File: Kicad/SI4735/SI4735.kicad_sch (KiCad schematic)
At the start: 128 parts, among them IC1 SI4732-A10-GS, IC2 TCA9537DGSR, J1 Conn_01x03, J2 Conn_01x05, J3 Headphones, J5 DISP LEFT, J6 DISP RIGHT, J7 Conn_01x02_Pin, J8 TYPE-C-31-M-12, J9 Conn_01x02_Pin, Q2 2N7002, Q3 2SK508G-K51-AE3-R, SW1 SW_Push, T1 TestPoint, T10 TestPoint, T11 TestPoint, T5 TestPoint, T6 TestPoint, T7 TestPoint, T8 TestPoint, T9 TestPoint, U1 HT-CT62, U11 RT9013, U2 BME690, U4 LSM6DS3, U5 TPA6130A2RTJTR, U6 RT9013, U7 MAX98357AETE+T, U8 MAX98357AETE+T, U9 Si4735-D60-GU, X1 X322525MMB4SI, Y1 Si5351A-B-GT, Y2 RV-3032-C7

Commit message: Add files via upload
- Rotation of SI4732 Radio
- Added Battery Charging IC TP4057
- Added Light Sensor VEML7700
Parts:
- removed C33: 100nF, Capacitor_SMD:C_0603_1608Metric, symbol Device:C_Small
- added C10: 1uF, Capacitor_SMD:C_0603_1608Metric, symbol Device:C_Small
- added IC2: VEML7700, VEML7700:VEML7700, symbol VEML7700-TR:VEML7700-TR
- added JP1: Jumper_2_Small_Open, Jumper:SolderJumper-2_P1.3mm_Open_RoundedPad1.0x1.5mm, symbol Jumper:Jumper_2_Small_Open
- added R41: 2k, Resistor_SMD:R_0603_1608Metric, symbol Device:R_Small
- added U12: TP4057, Package_TO_SOT_SMD:TSOT-23-6, symbol Battery_Management:TP4057
- C1: renamed from C49; LCSC Part Name (none) -> C14663
- C11: renamed from C41; LCSC Part Name (none) -> C1656
- C12: renamed from C8; LCSC Part Name (none) -> C96446
- C13: renamed from C9; LCSC Part Name (none) -> C96446
- C14: renamed from C10; LCSC Part Name (none) -> C96446
- C15: renamed from C11; LCSC Part Name (none) -> C96446
- C16: renamed from C43; LCSC Part Name (none) -> C1656
- C17: renamed from C46; LCSC Part Name (none) -> C1656
- C18: renamed from C48; LCSC Part Name (none) -> C1623
- C19: renamed from C47; LCSC Part Name (none) -> C1656
- C2: renamed from C44; LCSC Part Name (none) -> C14663
- C20: renamed from C14; LCSC Part Name (none) -> C15849
- C21: renamed from C15; LCSC Part Name (none) -> C15849
- C22: renamed from C18; LCSC Part Name (none) -> C14663
- C23: renamed from C19; LCSC Part Name (none) -> C14663
- C24: renamed from C20; LCSC Part Name (none) -> C15849
- C25: renamed from C21; LCSC Part Name (none) -> C14663
- C26: renamed from C23; LCSC Part Name (none) -> C14663
- C27: LCSC Part Name (none) -> C14663
- C28: renamed from C24; LCSC Part Name (none) -> C14663
- C3: renamed from C16; LCSC Part Name (none) -> C15849
- C30: renamed from C34; value 270p -> 330pF; LCSC Part Name (none) -> C1664
- C31: renamed from C37; LCSC Part Name (none) -> C14663
- C32: renamed from C42; LCSC Part Name (none) -> C1653
- C33: renamed from C39; value 270p -> 330pF; LCSC Part Name (none) -> C1664
- C34: renamed from C28; LCSC Part Name (none) -> C28323
- C36: renamed from C29; LCSC Part Name (none) -> C28323
- C37: renamed from C30; LCSC Part Name (none) -> C28323
- C4: renamed from C22; LCSC Part Name (none) -> C14663
- C5: renamed from C38; LCSC Part Name (none) -> C1656
- C6: renamed from C17; LCSC Part Name (none) -> C14663
- C7: renamed from C32; LCSC Part Name (none) -> C21122
- C8: renamed from C36; LCSC Part Name (none) -> C1647
- C9: renamed from C40; LCSC Part Name (none) -> C1656
- D1: renamed from D7; LCSC Part Name (none) -> N.C.
- D2: renamed from D6; LCSC Part Name (none) -> N.C.
- IC1: LCSC Part Name C2155558 -> C2155558
- J1, L7, U+1, U-1: LCSC Part Name (none) -> N.C.
- J2: renamed from J9; LCSC Part Name (none) -> N.C.
- J3: renamed from J7; LCSC Part Name (none) -> N.C.
- J5: renamed from J3; LCSC Part Name (none) -> N.C.
- J6: renamed from J2; LCSC Part Name (none) -> N.C.
- J7: renamed from J5; LCSC Part Name (none) -> N.C.
- J8: renamed from J6; LCSC Part Name (none) -> N.C.
- L1: renamed from L4; LCSC Part Name (none) -> C18221279
- L2: renamed from L1; LCSC Part Name (none) -> C373725
- L3: renamed from L2; LCSC Part Name (none) -> C373725
- L4: renamed from L6; LCSC Part Name (none) -> C373725
- L5: footprint Inductor_SMD:L_0805_2012Metric_Pad1.15x1.40mm_HandSolder -> Inductor_SMD:L_0603_1608Metric_Pad1.05x0.95mm_HandSolder
- L6: renamed from L3; LCSC Part Name (none) -> C373725
- Q2: value 2N7002 -> SI2302
- R1: renamed from R45; LCSC Part Name (none) -> C15402
- R10: renamed from R41; LCSC Part Name (none) -> C22975
- R12: renamed from R48; LCSC Part Name (none) -> N.C.
- R13: renamed from R1; LCSC Part Name (none) -> C25804
- R14: renamed from R24; LCSC Part Name (none) -> C25804
- R17: renamed from R25; LCSC Part Name (none) -> C25804
- R18: renamed from R38; value 2k -> 0R; LCSC Part Name (none) -> C15402
- R19: renamed from R23; LCSC Part Name (none) -> C15402
- R2: renamed from R46; footprint Resistor_SMD:R_0805_2012Metric_Pad1.20x1.40mm_HandSolder -> Resistor_SMD:R_0603_1608Metric; LCSC Part Name (none) -> C15402
- R20: renamed from R15; LCSC C17414 -> C17477; LCSC Part Name (none) -> C17477
- R21: renamed from R27; LCSC Part Name (none) -> N.C.
- R22: renamed from R13; LCSC Part Name (none) -> C25804
- R23: renamed from R12; LCSC Part Name (none) -> C25804
- R24: renamed from R8; LCSC Part Name (none) -> C15402
- R25: renamed from R9; LCSC Part Name (none) -> C15402
- R26: renamed from R10; LCSC Part Name (none) -> N.C.
- R27: renamed from R11; LCSC Part Name (none) -> N.C.
- R28: LCSC Part Name (none) -> C15402
- R29: renamed from R39; LCSC Part Name (none) -> C15402
- R3: renamed from R40; LCSC Part Name (none) -> C22975
- R31: renamed from R26; LCSC Part Name (none) -> C15402
- R32: renamed from R18; LCSC Part Name (none) -> C25804
- R34: LCSC Part Name (none) -> C25804
- R36: renamed from R2; LCSC Part Name (none) -> C15402
- R37: renamed from R53; LCSC Part Name (none) -> C15402
- R38: renamed from R20; LCSC Part Name (none) -> C25804
- R39: renamed from R52; LCSC Part Name (none) -> C25804
- R4: renamed from R16; LCSC Part Name (none) -> C25803
- R40: renamed from R47; LCSC Part Name (none) -> C25804
- R5: renamed from R7; LCSC Part Name (none) -> C25803
- R6: renamed from R14; LCSC Part Name (none) -> N.C.
- R9: renamed from R42; LCSC Part Name (none) -> C23228
- T1: renamed from T6; LCSC Part Name (none) -> N.C.
- T2: renamed from T5; LCSC Part Name (none) -> N.C.
- T3: renamed from T11; LCSC Part Name (none) -> N.C.
- T4: renamed from T1; LCSC Part Name (none) -> N.C.
- T5: renamed from T7; LCSC Part Name (none) -> N.C.
- T6: renamed from T8; LCSC Part Name (none) -> N.C.
- T7: renamed from T9; LCSC Part Name (none) -> N.C.
- T8: renamed from T10; LCSC Part Name (none) -> N.C.
- U2: renamed from U8; LCSC Part Name (none) -> C910544
- U5: renamed from U2; LCSC Part Name (none) -> C42431867
- U6: renamed from U13; LCSC Part Name (none) -> C19270550
- Y2: LCSC Part Name (none) -> C5127802
- renumbered ANT0 to ANT2, ANT5 to ANT3, C45 to C35, D2 to D3, IC2 to IC3, J8 to J4, Q3 to Q1, R50 to R11, R49 to R15, R51 to R16, R22 to R30, R19 to R33, R44 to R35, R21 to R7, R17 to R8, U9 to U1, U4 to U10, U7 to U3, U5 to U4, U6 to U7, U1 to U8, U11 to U9
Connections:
- net +3.3VA: now also IC2.2 (VDD)
- net +5V: now also C10.1, JP1.2 (B), U12.3 (BAT); no longer J4.A4 (VBUS), J4.A9 (VBUS), J4.B4 (VBUS), J4.B9 (VBUS)
- net GND: now also C10.2, IC2.3 (GND), R41.1, U12.2 (GND)
- net SCL: now also IC2.1 (SCL)
- net SDA: now also IC2.4 (SDA)
- net at C30.1, R26.2: no longer J5.1 (Pin_1)
- new net: R41.2, U12.6 (PROG)
- new net +5VD: J4.A4 (VBUS), J4.A9 (VBUS), J4.B4 (VBUS), J4.B9 (VBUS), JP1.1 (A), U12.4 (V_{CC})
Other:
- note added: "Light Sensor"
- note added: "R18 Pad Umbaubar auf Quarz mit 22pF"
- moved on the sheet: J5

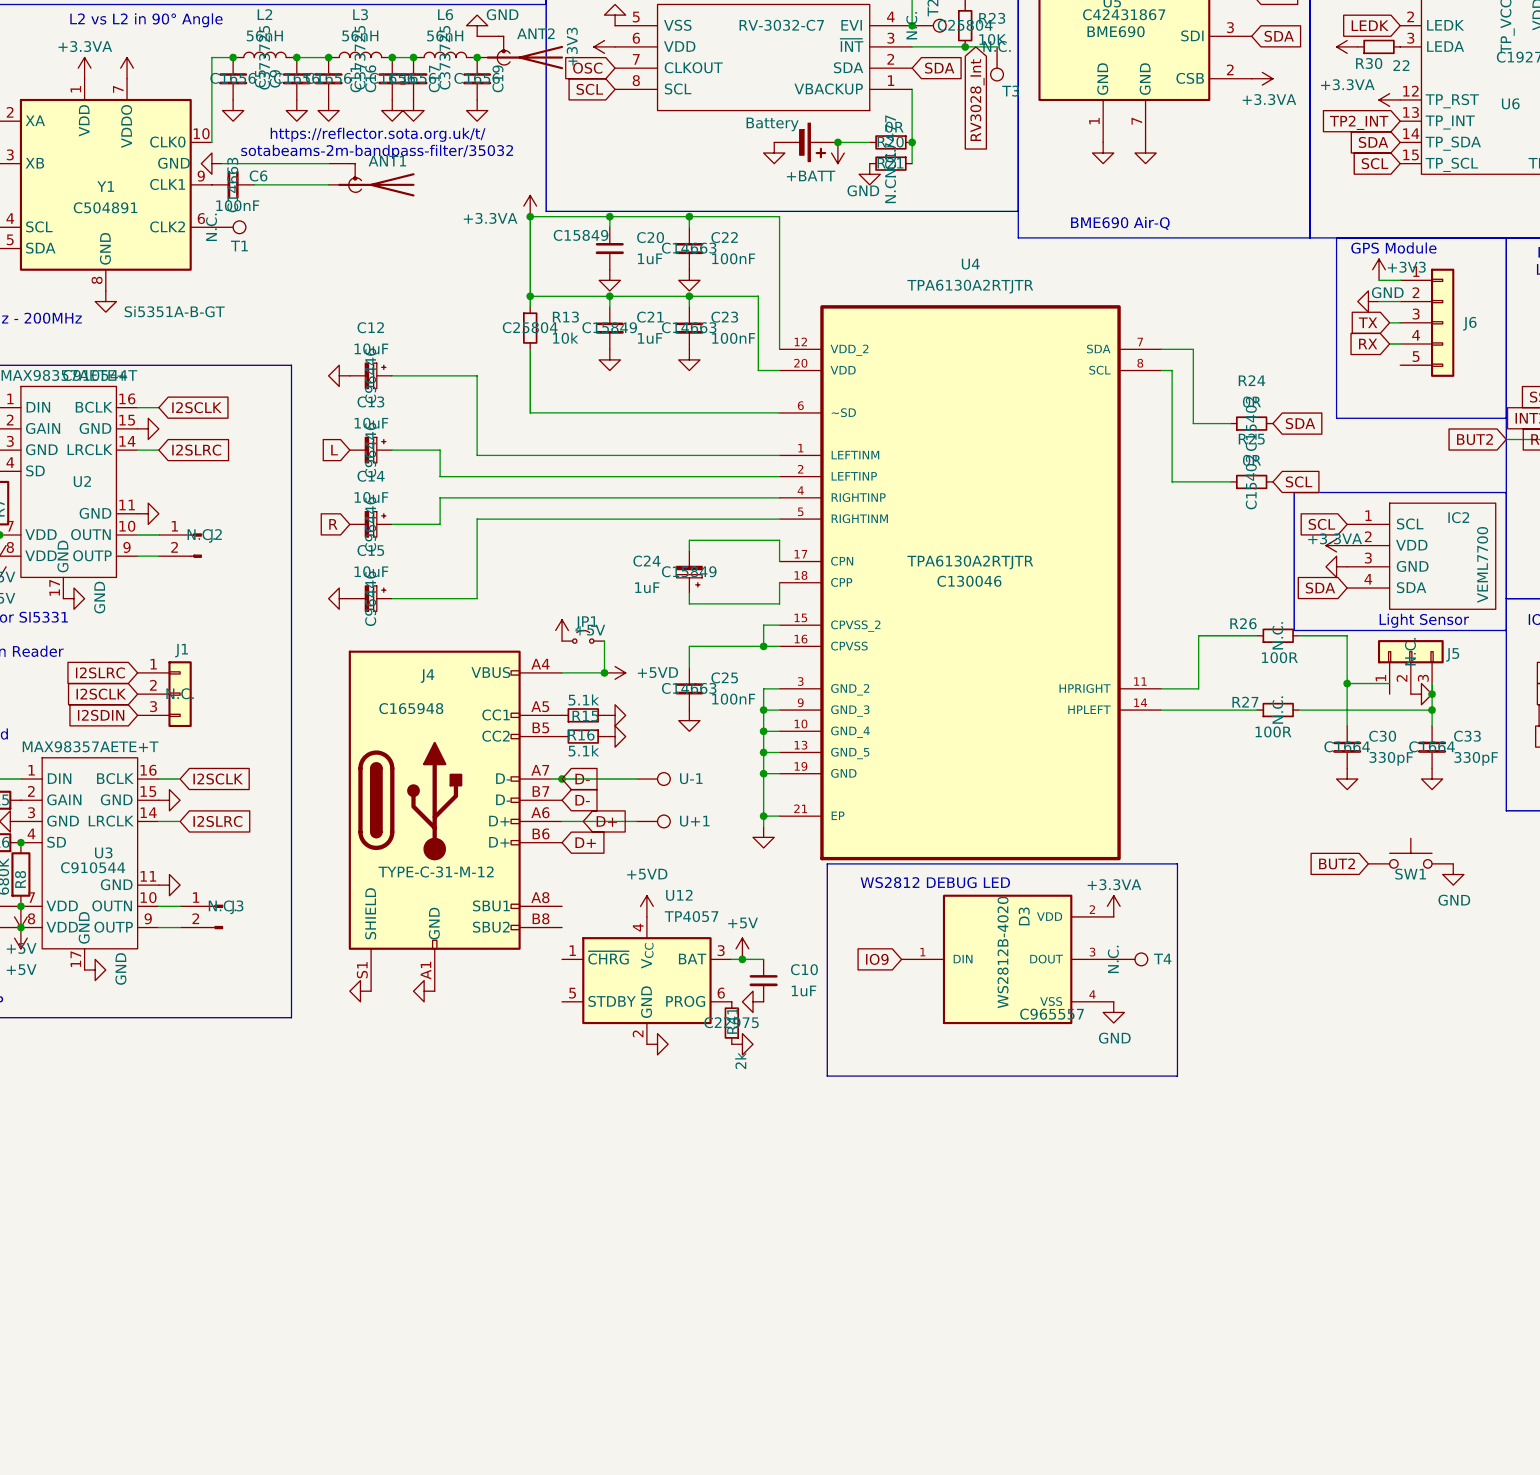
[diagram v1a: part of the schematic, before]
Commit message: Add files via upload
- Added MLX90640 Thermal Camera
- Refinement of inner Layers to enhance EMC
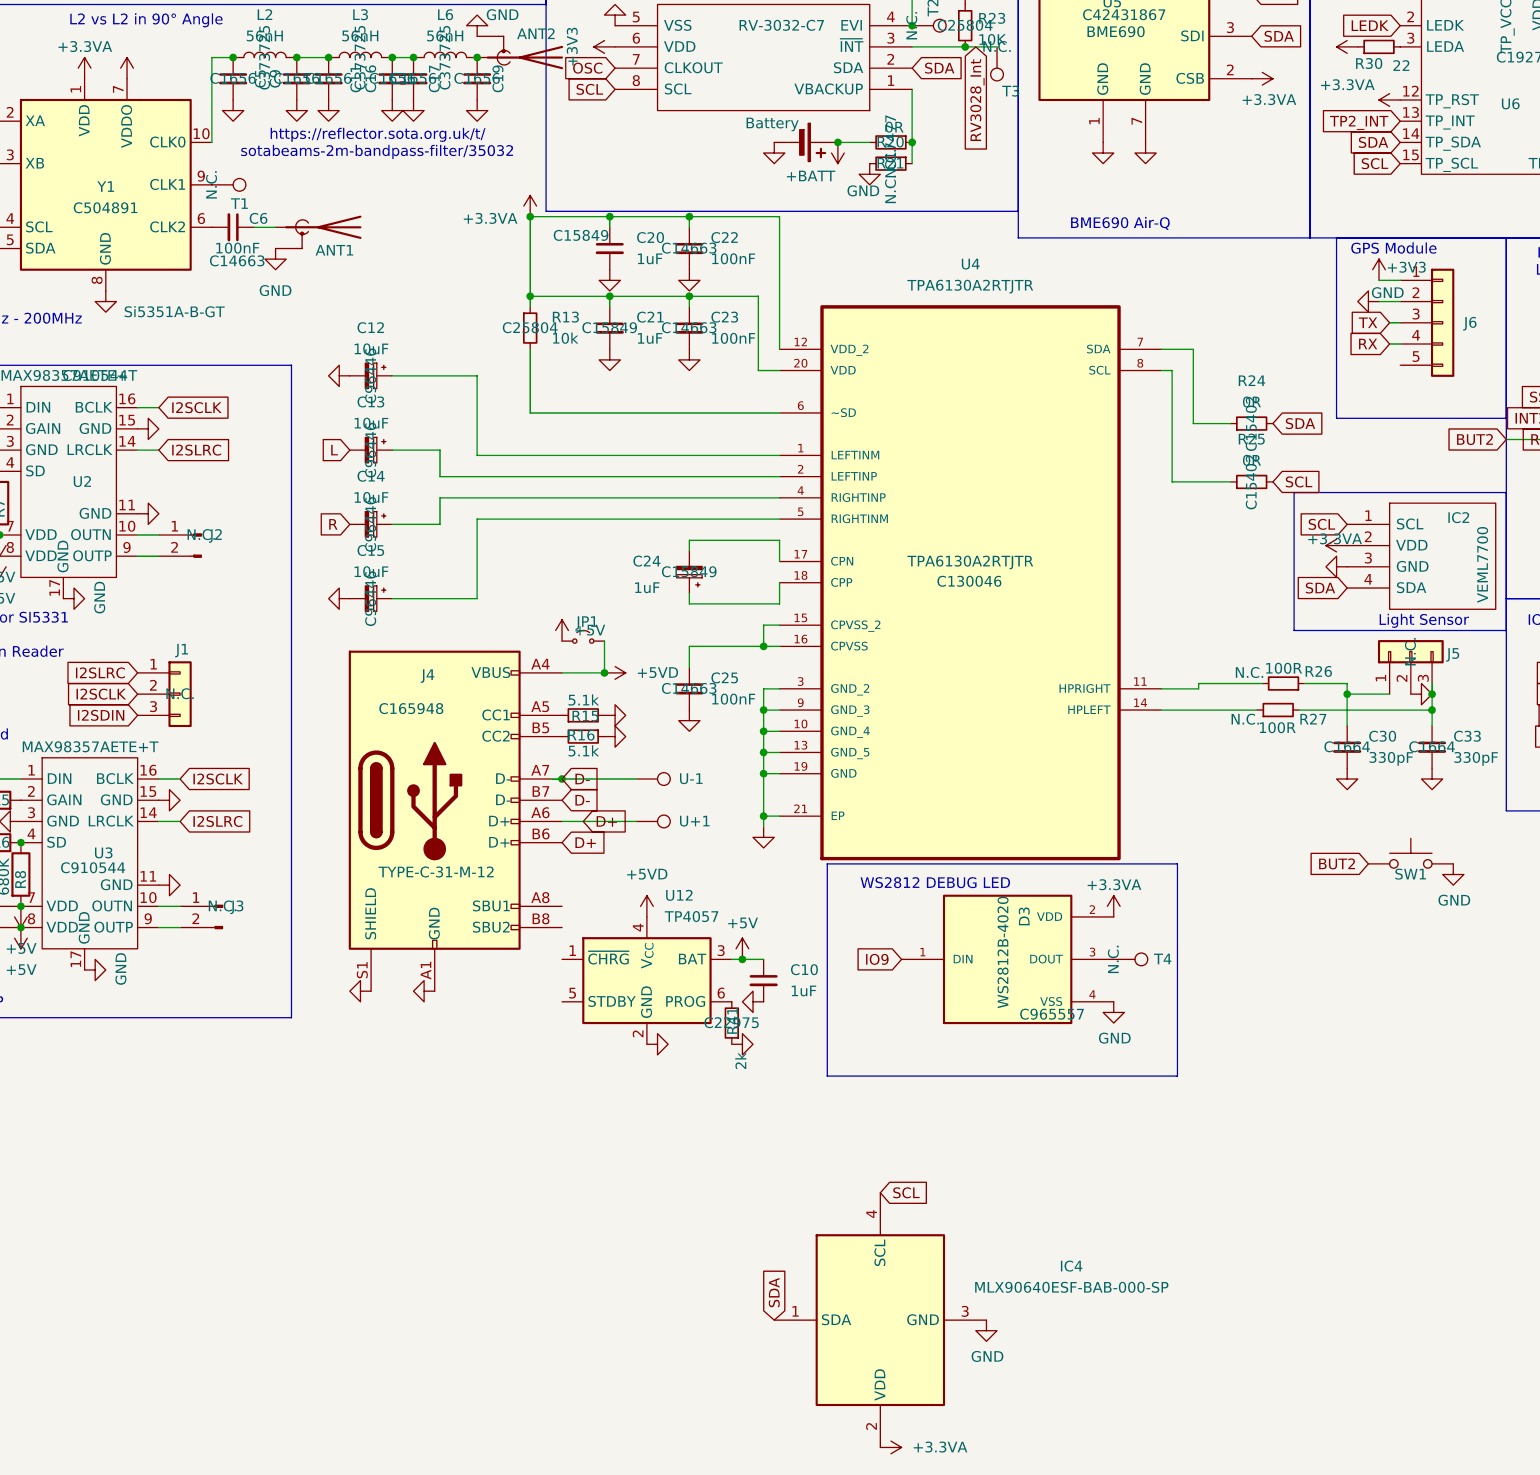
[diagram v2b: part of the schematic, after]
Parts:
- added IC4: MLX90640ESF-BAB-000-SP, MLX90640:MLX90640ESFBAB000SP, symbol MLX90640ESF-BAB-000-SP:MLX90640ESF-BAB-000-SP
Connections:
- net +3.3VA: now also IC4.2 (VDD)
- net GND: now also IC4.3 (GND)
- net SCL: now also IC4.4 (SCL)
- net SDA: now also IC4.1 (SDA)
- net at U4.11 (HPRIGHT): now also R26.2; no longer R26.1
- net at T1.1: now also Y1.9 (CLK1); no longer Y1.6 (CLK2)
- net at C30.1: now also J5.1 (Pin_1), R26.1; no longer R26.2
- net at C6.2: now also Y1.6 (CLK2); no longer Y1.9 (CLK1)
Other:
- moved on the sheet: ANT1, C6, R26, T1
